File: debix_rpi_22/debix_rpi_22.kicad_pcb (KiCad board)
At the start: 2 copper layers, 71 x 12.5 mm, 2 parts, among them J1 Conn_01x24, J3 RPi 22 Pin MIPI CSI-2

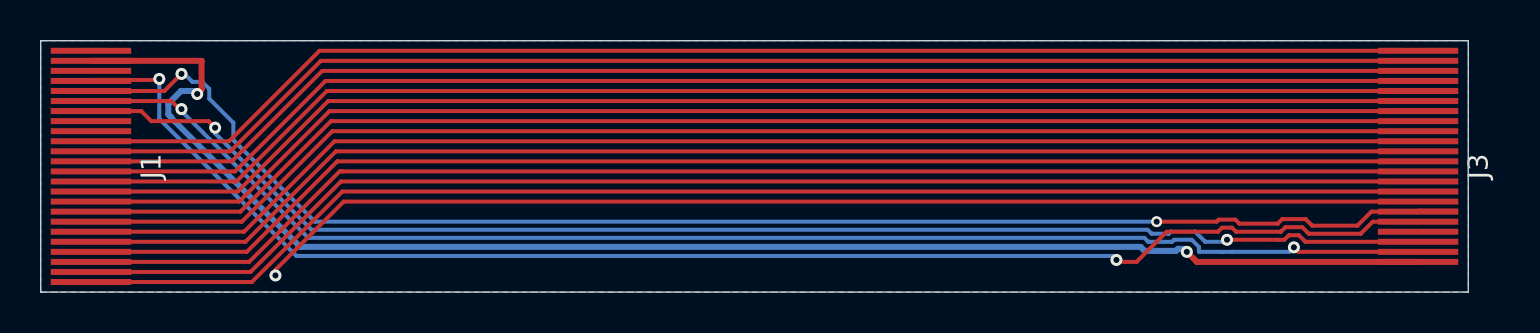
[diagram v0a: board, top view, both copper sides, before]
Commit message: got rid of the GND plane.
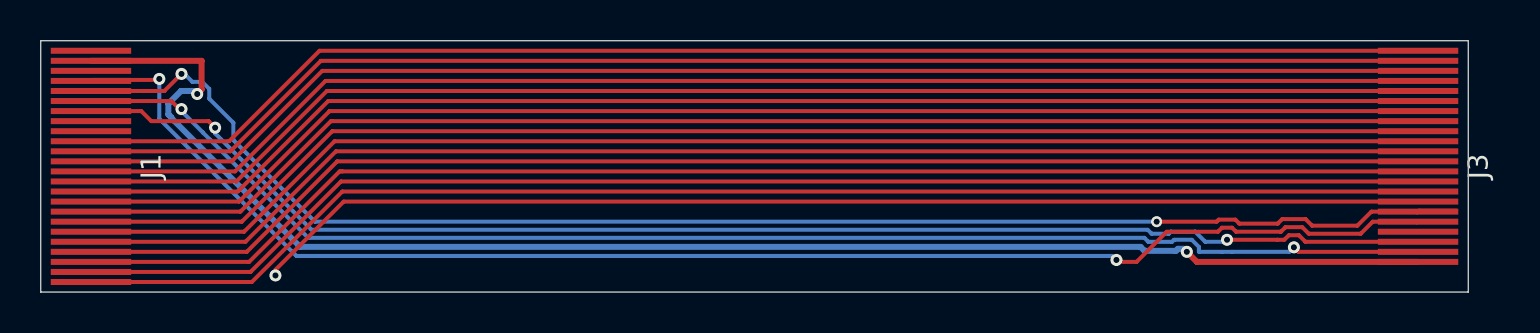
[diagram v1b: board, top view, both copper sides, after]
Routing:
- removed copper zone on B.Cu, net GND
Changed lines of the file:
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@@
-	)
-	(zone
-		(net 7)
-		(net_name "GND")
-		(layer "B.Cu")
-		(hatch edge 0.5)
-		(connect_pads
-			(clearance 0.5)
-		)
-		(min_thickness 0.25)
-		(filled_areas_thickness no)
-		(fill yes
-			(mode hatch)
-			(thermal_gap 0.5)
-			(thermal_bridge_width 0.5)
-			(island_removal_mode 1)
-			(island_area_min 10)
-			(hatch_thickness 0.5)
-			(hatch_gap 0.5)
-			(hatch_orientation 60)
-			(hatch_border_algorithm hatch_thickness)
-			(hatch_min_hole_area 0.3)
-		)
-		(polygon
-			(pts
-				(xy 180.5 129.5) (xy 180.5 142) (xy 109.5 142) (xy 109.5 129.5)
-			)
-		)
 	)
 	(zone

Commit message: moved all vias to other side.
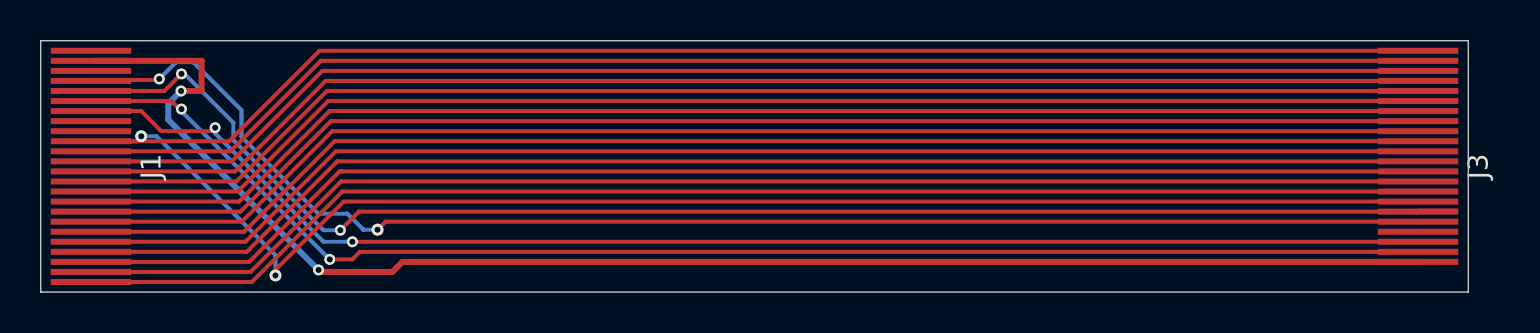
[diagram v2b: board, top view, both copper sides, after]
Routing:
- net GND: track 397.8 -> 408.6 mm, vias 1 -> 2
- net /CAM_GPIO_1: track 72.3 -> 70.8 mm

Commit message: rounded tracks...
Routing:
- net GND: track 408.6 -> 405.7 mm
- net +3V3: track 75.2 -> 74.6 mm
- net /CAM_GPIO_1: track 70.8 -> 70.3 mm
- net /csi_d3_P: track 67.9 -> 67.3 mm
- net /csi_d3_N: track 67.9 -> 67.3 mm
- net /csi_d2_P: track 67.9 -> 67.3 mm
- net /csi_clk_N: track 67.9 -> 67.3 mm
- net /csi_d2_N: track 67.9 -> 67.3 mm
- net /csi_d1_N: track 67.9 -> 67.3 mm
- net /csi_d0_P: track 67.9 -> 67.3 mm
- net /csi_d0_N: track 67.9 -> 67.3 mm
- net /csi_clk_P: track 67.9 -> 67.3 mm
- net /csi_d1_P: track 67.9 -> 67.3 mm

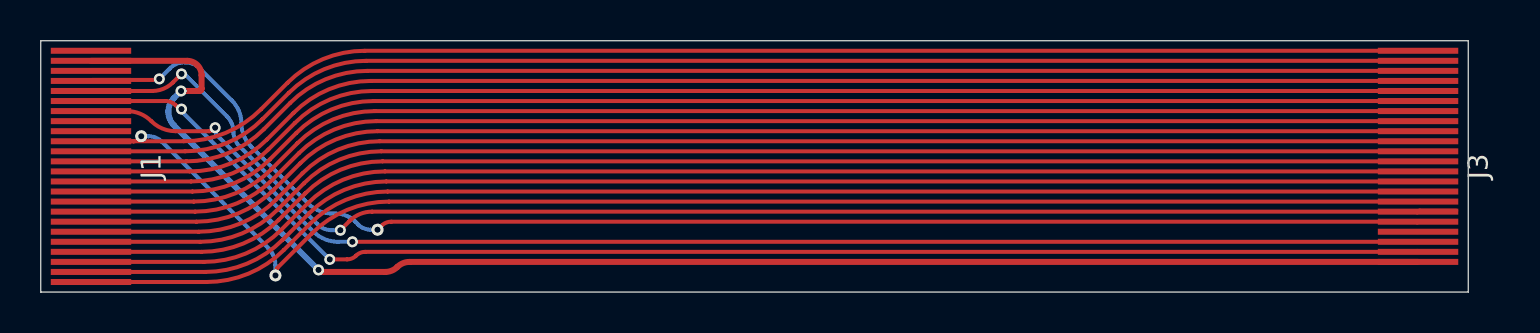
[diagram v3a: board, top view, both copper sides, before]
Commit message: shielded gpio enable und co from gpio
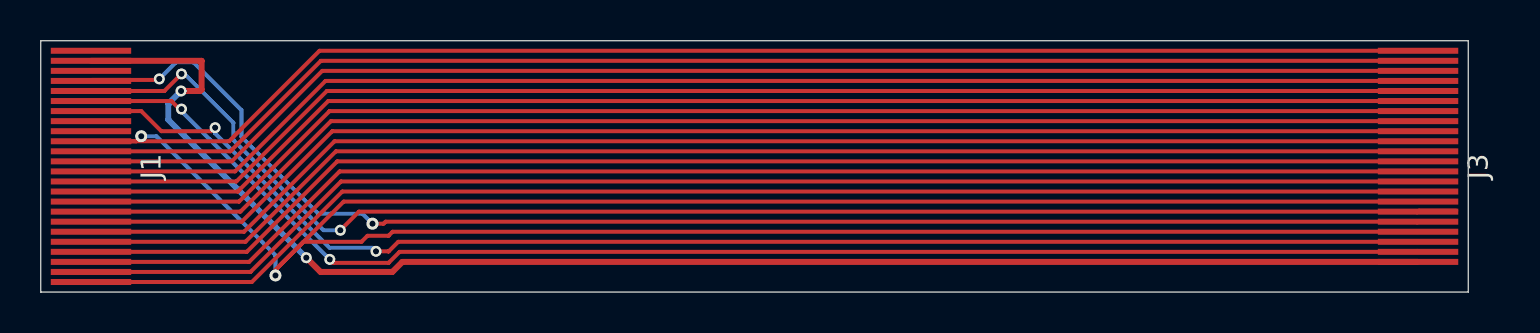
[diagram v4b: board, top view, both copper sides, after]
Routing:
- net GND: track 405.7 -> 466.2 mm
- net /csi_scl: track 68.7 -> 69.4 mm
- net +3V3: track 74.6 -> 75.2 mm
- net /csi_d3_P: track 67.3 -> 67.9 mm
- net /csi_d3_N: track 67.3 -> 67.9 mm
- net /csi_d2_P: track 67.3 -> 67.9 mm
- net /csi_clk_N: track 67.3 -> 67.9 mm
- net /csi_d2_N: track 67.3 -> 67.9 mm
- net /csi_d1_N: track 67.3 -> 67.9 mm
- net /csi_d0_P: track 67.3 -> 67.9 mm
- net /csi_d0_N: track 67.3 -> 67.9 mm
- net /csi_clk_P: track 67.3 -> 67.9 mm
- net /csi_d1_P: track 67.3 -> 67.9 mm

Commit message: ROUNDED.
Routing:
- net GND: track 466.2 -> 463.2 mm
- net +3V3: track 75.2 -> 74.6 mm
- net /csi_d3_P: track 67.9 -> 67.3 mm
- net /csi_d3_N: track 67.9 -> 67.3 mm
- net /csi_d2_P: track 67.9 -> 67.3 mm
- net /csi_clk_N: track 67.9 -> 67.3 mm
- net /csi_d2_N: track 67.9 -> 67.3 mm
- net /csi_d1_P: track 67.9 -> 67.3 mm
- net /csi_d1_N: track 67.9 -> 67.3 mm
- net /csi_d0_P: track 67.9 -> 67.3 mm
- net /csi_d0_N: track 67.9 -> 67.3 mm
- net /csi_clk_P: track 67.9 -> 67.3 mm

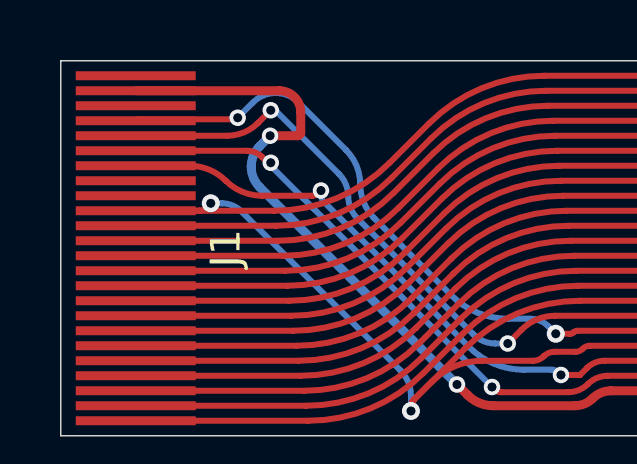
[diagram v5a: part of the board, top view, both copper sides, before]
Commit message: one teardrop missing and fixed weird tracks.
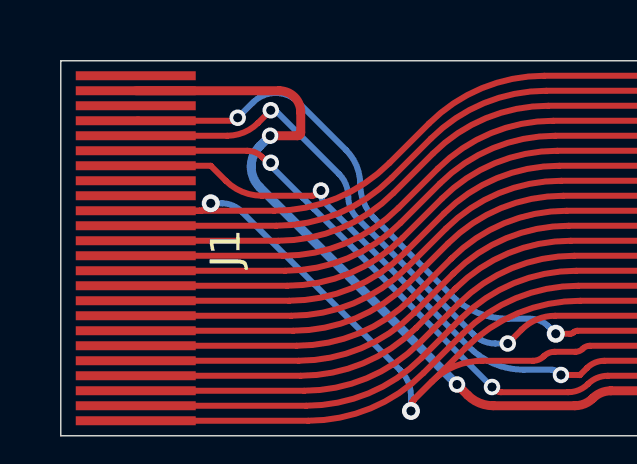
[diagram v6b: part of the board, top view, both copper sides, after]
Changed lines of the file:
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@@
 	)
 	(segment
+		(start 114.5 133)
+		(end 112 133)
+		(width 0.2)
+		(layer "F.Cu")
+		(net 1)
+	)
+	(segment
 		(start 127.041893 139.74095)
 		(end 126.804893 139.97795)
@@
 	)
 	(segment
-		(start 113.792893 133)
-		(end 112 133)
+		(start 127.623597 139.5)
+		(end 178 139.5)
 		(width 0.2)
 		(layer "F.Cu")
@@
 	)
 	(segment
-		(start 127.623597 139.5)
-		(end 178 139.5)
+		(start 126.174 139.974)
+		(end 126.787456 139.974)
 		(width 0.2)
 		(layer "F.Cu")
@@
 	)
 	(segment
-		(start 126.174 139.974)
-		(end 126.787456 139.974)
+		(start 115 133.5)
+		(end 114.5 133)
 		(width 0.2)
 		(layer "F.Cu")
@@
 	(arc
 		(start 115 133.5)
-		(mid 114.446174 133.129945)
-		(end 113.792893 133)
-		(width 0.2)
-		(layer "F.Cu")
-		(net 1)
-	)
-	(arc
-		(start 115 133.5)
 		(mid 115.553825 133.870054)
 		(end 116.207106 134)
@@
 		(drill 0.3)
 		(layers "F.Cu" "B.Cu")
+		(teardrops
+			(best_length_ratio 0.5)
+			(max_length 1)
+			(best_width_ratio 1)
+			(max_width 2)
+			(curved_edges no)
+			(filter_ratio 0.9)
+			(enabled yes)
+			(allow_two_segments yes)
+			(prefer_zone_connections yes)
+		)
 		(net 7)
 	)
@@
 	)
 	(segment
-		(start 115.310937 131.451)
-		(end 112.083648 131.451)
+		(start 126 138.6)
+		(end 126.480232 138.6)
 		(width 0.2)
 		(layer "F.Cu")
@@
 	)
 	(segment
-		(start 126 138.6)
-		(end 126.480232 138.6)
+		(start 177.9755 138.5245)
+		(end 177.951 138.549)
 		(width 0.2)
 		(layer "F.Cu")
@@
 	)
 	(segment
-		(start 177.9755 138.5245)
-		(end 177.951 138.549)
+		(start 115.298 131.5)
+		(end 115.398 131.4)
 		(width 0.2)
 		(layer "F.Cu")
@@
 	)
 	(segment
+		(start 112 131.5)
+		(end 115.298 131.5)
+		(width 0.2)
+		(layer "F.Cu")
+		(net 17)
+	)
+	(segment
 		(start 126.721653 138.5)
 		(end 177.965351 138.5)
@@
 	)
 	(zone
-		(net 17)
-		(net_name "/CAM_GPIO_1")
+		(net 1)
+		(net_name "/csi_scl")
 		(layer "F.Cu")
 		(name "$teardrop_padvia$")
 		(hatch full 0.1)
-		(priority 30005)
+		(priority 30009)
 		(attr
 			(teardrop
@@
 		(polygon
 			(pts
-				(xy 114.15 131.551) (xy 114.15 131.351) (xy 114 131.35) (xy 111.999 131.5) (xy 114 131.604455)
+				(xy 117.682209 133.9) (xy 117.682209 134.1) (xy 118.227915 134.095451) (xy 118.175265 133.825735)
+				(xy 118.021483 133.597081)
 			)
 		)
 	)
 	(zone
-		(net 1)
-		(net_name "/csi_scl")
+		(net 7)
+		(net_name "GND")
 		(layer "F.Cu")
 		(name "$teardrop_padvia$")
 		(hatch full 0.1)
-		(priority 30009)
+		(priority 30000)
 		(attr
 			(teardrop
@@
 		(polygon
 			(pts
-				(xy 117.682209 133.9) (xy 117.682209 134.1) (xy 118.227915 134.095451) (xy 118.175265 133.825735)
-				(xy 118.021483 133.597081)
+				(xy 114.15 134.6) (xy 114.15 134.4) (xy 114 134.35) (xy 111.999 134.5) (xy 114 134.65)
 			)
 		)
 	)
 	(zone
-		(net 7)
-		(net_name "GND")
+		(net 5)
+		(net_name "/csi_d2_P")
 		(layer "F.Cu")
 		(name "$teardrop_padvia$")
 		(hatch full 0.1)
-		(priority 30000)
+		(priority 30033)
 		(attr
 			(teardrop
@@
 		(polygon
 			(pts
-				(xy 114.15 134.6) (xy 114.15 134.4) (xy 114 134.35) (xy 111.999 134.5) (xy 114 134.65)
+				(xy 114.15 140.1) (xy 114.15 139.9) (xy 114 139.85) (xy 111.999 140) (xy 114 140.15)
 			)
 		)
 	)
 	(zone
-		(net 5)
-		(net_name "/csi_d2_P")
+		(net 16)
+		(net_name "/csi_d1_N")
 		(layer "F.Cu")
 		(name "$teardrop_padvia$")
 		(hatch full 0.1)
-		(priority 30033)
+		(priority 30000)
 		(attr
 			(teardrop
@@
 		(polygon
 			(pts
-				(xy 114.15 140.1) (xy 114.15 139.9) (xy 114 139.85) (xy 111.999 140) (xy 114 140.15)
+				(xy 175.85 131.9) (xy 175.85 132.1) (xy 176 132.15) (xy 178.001 132) (xy 176 131.85)
 			)
 		)
 	)
 	(zone
-		(net 16)
-		(net_name "/csi_d1_N")
+		(net 7)
+		(net_name "GND")
 		(layer "F.Cu")
 		(name "$teardrop_padvia$")
 		(hatch full 0.1)
-		(priority 30000)
+		(priority 30008)
 		(attr
 			(teardrop
@@
 		(polygon
 			(pts
-				(xy 175.85 131.9) (xy 175.85 132.1) (xy 176 132.15) (xy 178.001 132) (xy 176 131.85)
+				(xy 175.85 132.9) (xy 175.85 133.1) (xy 176 133.15) (xy 178.001 133) (xy 176 132.85)
 			)
 		)
 	)
 	(zone
-		(net 7)
-		(net_name "GND")
+		(net 17)
+		(net_name "/CAM_GPIO_1")
 		(layer "F.Cu")
 		(name "$teardrop_padvia$")
 		(hatch full 0.1)
-		(priority 30008)
+		(priority 30000)
 		(attr
 			(teardrop
@@
 		(polygon
 			(pts
-				(xy 175.85 132.9) (xy 175.85 133.1) (xy 176 133.15) (xy 178.001 133) (xy 176 132.85)
+				(xy 114.15 131.6) (xy 114.15 131.4) (xy 114 131.35) (xy 111.999 131.5) (xy 114 131.65)
 			)
 		)
@@
 	)
 	(zone
+		(net 7)
+		(net_name "GND")
+		(layer "F.Cu")
+		(name "$teardrop_padvia$")
+		(hatch full 0.1)
+		(priority 30001)
+		(attr
+			(teardrop
+				(type padvia)
+			)
+		)
+		(connect_pads yes
+			(clearance 0)
+		)
+		(min_thickness 0.0254)
+		(filled_areas_thickness no)
+		(fill yes
+			(thermal_gap 0.5)
+			(thermal_bridge_width 0.5)
+			(island_removal_mode 1)
+			(island_area_min 10)
+		)
+		(polygon
+			(pts
+				(xy 114.368112 134.4) (xy 114.368112 134.6) (xy 114.558524 134.546239) (xy 114.500997 134.252003)
+				(xy 114.250556 134.418674)
+			)
+		)
+	)
+	(zone
 		(net 4)
 		(net_name "/csi_sda")
@@
 	)
 	(zone
+		(net 1)
+		(net_name "/csi_scl")
+		(layer "F.Cu")
+		(name "$teardrop_padvia$")
+		(hatch full 0.1)
+		(priority 30000)
+		(attr
+			(teardrop
+				(type padvia)
+			)
+		)
+		(connect_pads yes
+			(clearance 0)
+		)
+		(min_thickness 0.0254)
+		(filled_areas_thickness no)
+		(fill yes
+			(thermal_gap 0.5)
+			(thermal_bridge_width 0.5)
+			(island_removal_mode 1)
+			(island_area_min 10)
+		)
+		(polygon
+			(pts
+				(xy 114.15 133.1) (xy 114.15 132.9) (xy 114 132.85) (xy 111.999 133) (xy 114 133.15)
+			)
+		)
+	)
+	(zone
 		(net 12)
 		(net_name "/csi_d3_P")
@@
 	)
 	(zone
+		(net 7)
+		(net_name "GND")
+		(layer "F.Cu")
+		(name "$teardrop_padvia$")
+		(hatch full 0.1)
+		(priority 30000)
+		(attr
+			(teardrop
+				(type padvia)
+			)
+		)
+		(connect_pads yes
+			(clearance 0)
+		)
+		(min_thickness 0.0254)
+		(filled_areas_thickness no)
+		(fill yes
+			(thermal_gap 0.5)
+			(thermal_bridge_width 0.5)
+			(island_removal_mode 1)
+			(island_area_min 10)
+		)
+		(polygon
+			(pts
+				(xy 114.258302 134.6) (xy 114.258302 134.4) (xy 114.205761 134.31053) (xy 114.498997 134.252003)
+				(xy 114.558524 134.546239)
+			)
+		)
+	)
+	(zone
 		(net 4)
 		(net_name "/csi_sda")
@@
 	)
 	(zone
+		(net 17)
+		(net_name "/CAM_GPIO_1")
+		(layer "F.Cu")
+		(name "$teardrop_padvia$")
+		(hatch full 0.1)
+		(priority 30001)
+		(attr
+			(teardrop
+				(type padvia)
+			)
+		)
+		(connect_pads yes
+			(clearance 0)
+		)
+		(min_thickness 0.0254)
+		(filled_areas_thickness no)
+		(fill yes
+			(thermal_gap 0.5)
+			(thermal_bridge_width 0.5)
+			(island_removal_mode 1)
+			(island_area_min 10)
+		)
+		(polygon
+			(pts
+				(xy 114.872483 131.4) (xy 114.872483 131.6) (xy 115.34435 131.669716) (xy 115.399 131.4) (xy 115.245218 131.171346)
+			)
+		)
+	)
+	(zone
 		(net 6)
 		(net_name "/csi_d1_P")
@@
 		(polygon
 			(pts
-				(xy 115.853883 131.085539) (xy 115.712461 130.944117) (xy 115.245218 131.171346) (xy 115.397293 131.400707)
+				(xy 115.853882 131.085538) (xy 115.712461 130.944117) (xy 115.245218 131.171346) (xy 115.397293 131.400707)
 				(xy 115.626654 131.552782)
 			)
@@
 			)
 		)
+	)
+	(zone
+		(net 7)
+		(net_name "GND")
+		(layer "B.Cu")
+		(name "$teardrop_padvia$")
+		(hatch full 0.1)
+		(priority 30000)
+		(attr
+			(teardrop
+				(type padvia)
+			)
+		)
+		(connect_pads yes
+			(clearance 0)
+		)
+		(min_thickness 0.0254)
+		(filled_areas_thickness no)
+		(fill yes
+			(thermal_gap 0.5)
+			(thermal_bridge_width 0.5)
+			(island_removal_mode 1)
+			(island_area_min 10)
+		)
+		(polygon
+			(pts
+				(xy 114.992039 134.361255) (xy 115.031055 134.165099) (xy 114.666668 134.002562) (xy 114.499017 134.251808)
+				(xy 114.666668 134.501444)
+			)
+		)
